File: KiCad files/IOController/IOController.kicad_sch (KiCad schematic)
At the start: 12 parts, among them J1 AVR-ISP-6, J2 Conn_01x01, J3 Conn_01x01, J4 Conn_01x01, J5 Conn_01x01, Q1 IRF3205, U1 ATtiny85-20P, U2 LP2985-5.0

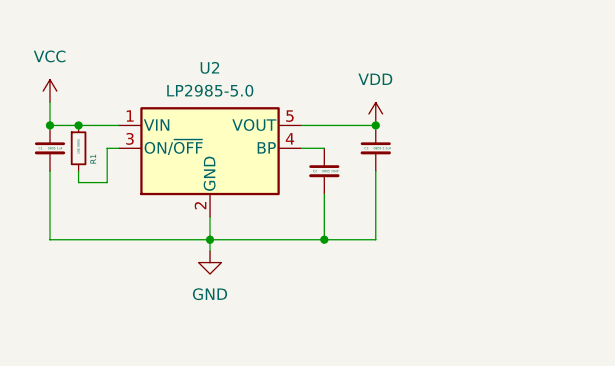
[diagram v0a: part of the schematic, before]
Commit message: swapped regulator for 1.8V instead of 5V for lower power
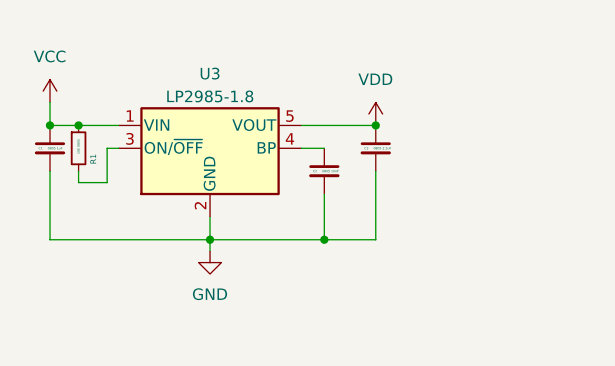
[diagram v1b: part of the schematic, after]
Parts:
- removed U2: LP2985-5.0, Package_TO_SOT_SMD:SOT-23-5, symbol Regulator_Linear:LP2985-5.0
- added U3: LP2985-1.8, Package_TO_SOT_SMD:SOT-23-5, symbol Regulator_Linear:LP2985-1.8
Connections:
- net GND: now also U3.2 (GND)
- net VCC: now also U3.1 (VIN)
- net VDD: now also U3.5 (VOUT)
- net at C2.1: now also U3.4 (BP)
- net at R1.2: now also U3.3 (ON/~{OFF})
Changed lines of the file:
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@@
+    )
+  )
+  (symbol (lib_id "Regulator_Linear:LP2985-1.8") (at 41.91 25.4 0) (unit 1)
+    (in_bom yes) (on_board yes) (dnp no) (fields_autoplaced)
+    (property "Reference" "U3" (at 41.91 17.145 0)
+      (effects (font (size 1.27 1.27)))
+    )
+    (property "Value" "LP2985-1.8" (at 41.91 19.685 0)
+      (effects (font (size 1.27 1.27)))
+    )
+    (property "Footprint" "Package_TO_SOT_SMD:SOT-23-5" (at 41.91 17.145 0)
+      (effects (font (size 1.27 1.27)) hide)
+    )
+    (property "Datasheet" "http://www.ti.com/lit/ds/symlink/lp2985.pdf" (at 41.91 25.4 0)
+      (effects (font (size 1.27 1.27)) hide)
+    )
+    (pin "3")
+    (pin "5")
+    (pin "4")
+    (pin "2")
+    (pin "1")
+    (instances
+      (project "IOController"
+        (path "/f1c719f6-f1ad-4e81-8891-bde8a483290d"
+          (reference "U3") (unit 1)
+        )
+      )
     )
   )
@@
         )
       )
-    )
-  )
-  (symbol (lib_id "Regulator_Linear:LP2985-5.0") (at 41.91 25.4 0) (unit 1)
-    (in_bom yes) (on_board yes) (dnp no) (fields_autoplaced)
-    (property "Reference" "U2" (at 41.91 16.51 0)
-      (effects (font (size 1.27 1.27)))
-    )
-    (property "Value" "LP2985-5.0" (at 41.91 19.05 0)
-      (effects (font (size 1.27 1.27)))
-    )
-    (property "Footprint" "Package_TO_SOT_SMD:SOT-23-5" (at 41.91 17.145 0)
-      (effects (font (size 1.27 1.27)) hide)
-    )
-    (property "Datasheet" "http://www.ti.com/lit/ds/symlink/lp2985.pdf" (at 41.91 25.4 0)
-      (effects (font (size 1.27 1.27)) hide)
-    )
-    (pin "4")
-    (pin "3")
-    (pin "2")
-    (pin "5")
-    (pin "1")
-    (instances
-      (project "IOController"
-        (path "/f1c719f6-f1ad-4e81-8891-bde8a483290d"
-          (reference "U2") (unit 1)
-        )
-      )

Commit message: added some parts to controller board for now.
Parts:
- removed J5: Conn_01x01, Connector_Wire:SolderWire-2.5sqmm_1x01_D2.4mm_OD3.6mm, symbol Connector_Generic:Conn_01x01
- removed Q1: IRF3205, Package_TO_SOT_THT:TO-220-3_Vertical, symbol Transistor_FET:IRF3205
- added J6: Conn_01x01, Connector_Wire:SolderWire-2.5sqmm_1x01_D2.4mm_OD3.6mm, symbol Connector_Generic:Conn_01x01
- added SW1: RotaryEncoder_Switch, Rotary_Encoder:RotaryEncoder_Bourns_Horizontal_PEC09-2xxxF-Nxxxx, symbol Device:RotaryEncoder_Switch
- added SW2: SW_Push, symbol Switch:SW_Push
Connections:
- net NPN-Gate: now also J6.1 (Pin_1)
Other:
- moved on the sheet: J2
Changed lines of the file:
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@@
+    (stroke (width 0) (type default))
+  )
+  (wire (pts (xy 146.05 34.29) (xy 146.05 32.385))
     (stroke (width 0) (type default))
   )
@@
     (stroke (width 0) (type default))
   )
-  (wire (pts (xy 135.89 25.4) (xy 135.89 23.495))
+  (wire (pts (xy 135.89 34.29) (xy 135.89 32.385))
     (stroke (width 0) (type default))
   )
@@
     (stroke (width 0) (type default))
   )
-  (wire (pts (xy 146.05 25.4) (xy 146.05 23.495))
-    (stroke (width 0) (type default))
-  )
   (wire (pts (xy 76.2 76.835) (xy 65.405 76.835))
     (stroke (width 0) (type default))
@@
     (stroke (width 0) (type default))
   )
-  (global_label "NPN-Gate" (shape input) (at 146.05 36.83 180) (fields_autoplaced)
-    (effects (font (size 1.27 1.27)) (justify right))
-    (property "Intersheetrefs" "${INTERSHEET_REFS}" (at 133.3281 36.83 0)
-      (effects (font (size 1.27 1.27)) (justify right) hide)
-    )
-  )
-  (global_label "LED_GND" (shape input) (at 153.67 31.75 90) (fields_autoplaced)
+  (global_label "NPN-Gate" (shape input) (at 146.05 32.385 90) (fields_autoplaced)
     (effects (font (size 1.27 1.27)) (justify left))
-    (property "Intersheetrefs" "${INTERSHEET_REFS}" (at 153.67 20.4796 90)
+    (property "Intersheetrefs" "${INTERSHEET_REFS}" (at 146.05 19.6631 90)
       (effects (font (size 1.27 1.27)) (justify left) hide)
     )
@@
     )
   )
-  (global_label "LED_GND" (shape input) (at 146.05 23.495 90) (fields_autoplaced)
-    (effects (font (size 1.27 1.27)) (justify left))
-    (property "Intersheetrefs" "${INTERSHEET_REFS}" (at 146.05 12.2246 90)
+  (symbol (lib_id "Connector_Generic:Conn_01x01") (at 135.89 39.37 270) (unit 1)
+    (in_bom yes) (on_board yes) (dnp no)
+    (property "Reference" "J2" (at 138.43 38.1 90)
+      (effects (font (size 1.27 1.27)) (justify left))
+    )
+    (property "Value" "Conn_01x01" (at 138.43 40.64 90)
       (effects (font (size 1.27 1.27)) (justify left) hide)
     )
-  )
-  (symbol (lib_id "Connector_Generic:Conn_01x01") (at 135.89 30.48 270) (unit 1)
-    (in_bom yes) (on_board yes) (dnp no) (fields_autoplaced)
-    (property "Reference" "J2" (at 138.43 29.21 90)
-      (effects (font (size 1.27 1.27)) (justify left))
-    )
-    (property "Value" "Conn_01x01" (at 138.43 31.75 90)
-      (effects (font (size 1.27 1.27)) (justify left) hide)
-    )
-    (property "Footprint" "Connector_Wire:SolderWire-2.5sqmm_1x01_D2.4mm_OD3.6mm" (at 135.89 30.48 0)
-      (effects (font (size 1.27 1.27)) hide)
-    )
-    (property "Datasheet" "~" (at 135.89 30.48 0)
+    (property "Footprint" "Connector_Wire:SolderWire-2.5sqmm_1x01_D2.4mm_OD3.6mm" (at 135.89 39.37 0)
+      (effects (font (size 1.27 1.27)) hide)
+    )
+    (property "Datasheet" "~" (at 135.89 39.37 0)
       (effects (font (size 1.27 1.27)) hide)
     )
@@
     )
   )
+  (symbol (lib_id "Switch:SW_Push") (at 132.08 98.425 0) (unit 1)
+    (in_bom yes) (on_board yes) (dnp no) (fields_autoplaced)
+    (property "Reference" "SW2" (at 132.08 90.17 0)
+      (effects (font (size 1.27 1.27)))
+    )
+    (property "Value" "SW_Push" (at 132.08 92.71 0)
+      (effects (font (size 1.27 1.27)))
+    )
+    (property "Footprint" "" (at 132.08 93.345 0)
+      (effects (font (size 1.27 1.27)) hide)
+    )
+    (property "Datasheet" "~" (at 132.08 93.345 0)
+      (effects (font (size 1.27 1.27)) hide)
+    )
+    (pin "2")
+    (pin "1")
+    (instances
+      (project "IOController"
+        (path "/f1c719f6-f1ad-4e81-8891-bde8a483290d"
+          (reference "SW2") (unit 1)
+        )
+      )
+    )
+  )
   (symbol (lib_id "power:GND") (at 50.165 86.995 0) (unit 1)
     (in_bom yes) (on_board yes) (dnp no) (fields_autoplaced)
@@
         (path "/f1c719f6-f1ad-4e81-8891-bde8a483290d"
           (reference "#PWR02") (unit 1)
-        )
-      )
-    )
-  )
-  (symbol (lib_id "Connector_Generic:Conn_01x01") (at 146.05 30.48 270) (unit 1)
-    (in_bom yes) (on_board yes) (dnp no) (fields_autoplaced)
-    (property "Reference" "J5" (at 148.59 29.21 90)
-      (effects (font (size 1.27 1.27)) (justify left))
-    )
-    (property "Value" "Conn_01x01" (at 148.59 31.75 90)
-      (effects (font (size 1.27 1.27)) (justify left) hide)
-    )
-    (property "Footprint" "Connector_Wire:SolderWire-2.5sqmm_1x01_D2.4mm_OD3.6mm" (at 146.05 30.48 0)
-      (effects (font (size 1.27 1.27)) hide)
-    )
-    (property "Datasheet" "~" (at 146.05 30.48 0)
-      (effects (font (size 1.27 1.27)) hide)
-    )
-    (pin "1")
-    (instances
-      (project "IOController"
-        (path "/f1c719f6-f1ad-4e81-8891-bde8a483290d"
-          (reference "J5") (unit 1)
         )
       )
@@
     )
   )
-  (symbol (lib_id "power:VCC") (at 135.89 23.495 0) (unit 1)
-    (in_bom yes) (on_board yes) (dnp no) (fields_autoplaced)
-    (property "Reference" "#PWR08" (at 135.89 27.305 0)
-      (effects (font (size 1.27 1.27)) hide)
-    )
-    (property "Value" "VCC" (at 135.89 18.415 0)
-      (effects (font (size 1.27 1.27)))
-    )
-    (property "Footprint" "" (at 135.89 23.495 0)
-      (effects (font (size 1.27 1.27)) hide)
-    )
-    (property "Datasheet" "" (at 135.89 23.495 0)
+  (symbol (lib_id "power:VCC") (at 135.89 32.385 0) (unit 1)
+    (in_bom yes) (on_board yes) (dnp no) (fields_autoplaced)
+    (property "Reference" "#PWR08" (at 135.89 36.195 0)
+      (effects (font (size 1.27 1.27)) hide)
+    )
+    (property "Value" "VCC" (at 135.89 27.305 0)
+      (effects (font (size 1.27 1.27)))
+    )
+    (property "Footprint" "" (at 135.89 32.385 0)
+      (effects (font (size 1.27 1.27)) hide)
+    )
+    (property "Datasheet" "" (at 135.89 32.385 0)
       (effects (font (size 1.27 1.27)) hide)
     )
@@
     )
   )
-  (symbol (lib_id "Transistor_FET:IRF3205") (at 151.13 36.83 0) (unit 1)
-    (in_bom yes) (on_board yes) (dnp no) (fields_autoplaced)
-    (property "Reference" "Q1" (at 157.48 35.56 0)
+  (symbol (lib_id "Connector_Generic:Conn_01x01") (at 146.05 39.37 270) (unit 1)
+    (in_bom yes) (on_board yes) (dnp no)
+    (property "Reference" "J6" (at 148.59 38.1 90)
       (effects (font (size 1.27 1.27)) (justify left))
     )
-    (property "Value" "IRF3205" (at 157.48 38.1 0)
-      (effects (font (size 1.27 1.27)) (justify left))
-    )
-    (property "Footprint" "Package_TO_SOT_THT:TO-220-3_Vertical" (at 156.21 38.735 0)
-      (effects (font (size 1.27 1.27) italic) (justify left) hide)
-    )
-    (property "Datasheet" "http://www.irf.com/product-info/datasheets/data/irf3205.pdf" (at 156.21 40.64 0)
+    (property "Value" "Conn_01x01" (at 148.59 40.64 90)
       (effects (font (size 1.27 1.27)) (justify left) hide)
     )
-    (pin "2")
-    (pin "1")
-    (pin "3")
-    (instances
-      (project "IOController"
-        (path "/f1c719f6-f1ad-4e81-8891-bde8a483290d"
-          (reference "Q1") (unit 1)
+    (property "Footprint" "Connector_Wire:SolderWire-2.5sqmm_1x01_D2.4mm_OD3.6mm" (at 146.05 39.37 0)
+      (effects (font (size 1.27 1.27)) hide)
+    )
+    (property "Datasheet" "~" (at 146.05 39.37 0)
+      (effects (font (size 1.27 1.27)) hide)
+    )
+    (pin "1")
+    (instances
+      (project "IOController"
+        (path "/f1c719f6-f1ad-4e81-8891-bde8a483290d"
+          (reference "J6") (unit 1)
         )
       )
@@
     )
   )
+  (symbol (lib_id "Device:RotaryEncoder_Switch") (at 117.475 79.375 90) (unit 1)
+    (in_bom yes) (on_board yes) (dnp no) (fields_autoplaced)
+    (property "Reference" "SW1" (at 124.46 78.105 90)
+      (effects (font (size 1.27 1.27)) (justify right))
+    )
+    (property "Value" "RotaryEncoder_Switch" (at 124.46 80.645 90)
+      (effects (font (size 1.27 1.27)) (justify right))
+    )
+    (property "Footprint" "Rotary_Encoder:RotaryEncoder_Bourns_Horizontal_PEC09-2xxxF-Nxxxx" (at 113.411 83.185 0)
+      (effects (font (size 1.27 1.27)) hide)
+    )
+    (property "Datasheet" "~" (at 110.871 79.375 0)
+      (effects (font (size 1.27 1.27)) hide)
+    )
+    (pin "S2")
+    (pin "B")
+    (pin "S1")
+    (pin "A")
+    (pin "C")
+    (instances
+      (project "IOController"
+        (path "/f1c719f6-f1ad-4e81-8891-bde8a483290d"
+          (reference "SW1") (unit 1)
+        )
+      )
+    )
+  )
   (symbol (lib_id "power:VDD") (at 50.165 56.515 0) (unit 1)
     (in_bom yes) (on_board yes) (dnp no) (fields_autoplaced)
@@
         )
       )
-    )
-  )
-  (symbol (lib_id "power:GND") (at 153.67 41.91 0) (unit 1)
-    (in_bom yes) (on_board yes) (dnp no) (fields_autoplaced)
-    (property "Reference" "#PWR011" (at 153.67 48.26 0)
-      (effects (font (size 1.27 1.27)) hide)
-    )
-    (property "Value" "GND" (at 153.67 46.99 0)
-      (effects (font (size 1.27 1.27)))
-    )
-    (property "Footprint" "" (at 153.67 41.91 0)
-      (effects (font (size 1.27 1.27)) hide)
-    )
-    (property "Datasheet" "" (at 153.67 41.91 0)
-      (effects (font (size 1.27 1.27)) hide)
-    )
-    (pin "1")
-    (instances
-      (project "IOController"
-        (path "/f1c719f6-f1ad-4e81-8891-bde8a483290d"
-          (reference "#PWR011") (unit 1)
-        )
-      )

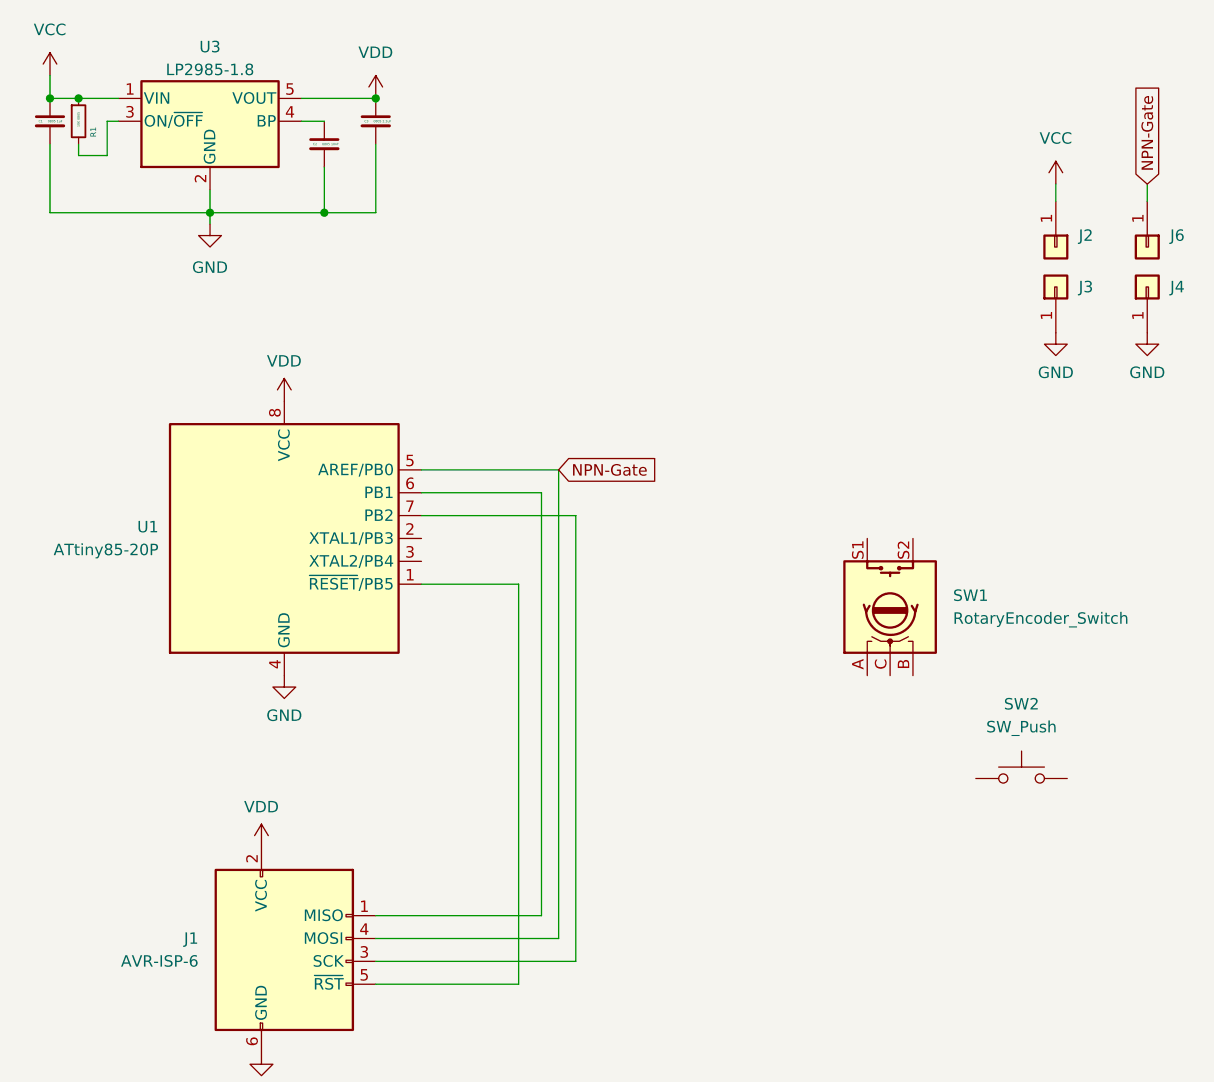
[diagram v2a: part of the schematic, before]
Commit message: modified IO board and LED board so they connect together using XT60
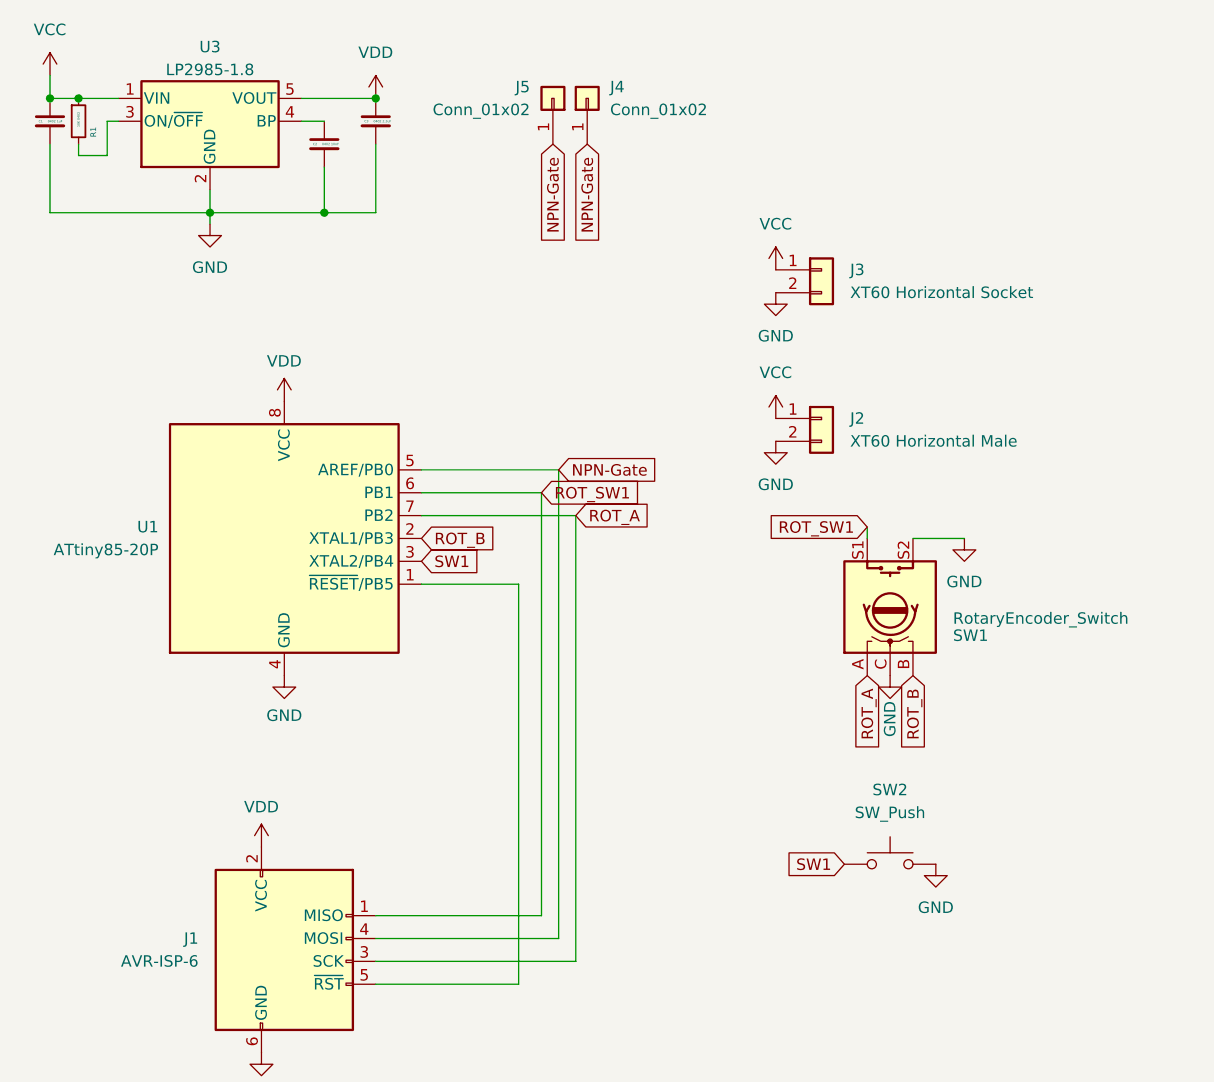
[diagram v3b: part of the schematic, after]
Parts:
- removed J2, J3, J6: Conn_01x01, Connector_Wire:SolderWire-2.5sqmm_1x01_D2.4mm_OD3.6mm, symbol Connector_Generic:Conn_01x01
- added J2: XT60 Horizontal Male, Connector_AMASS:AMASS_XT60PW-M_1x02_P7.20mm_Horizontal, symbol Connector_Generic:Conn_01x02
- added J3: XT60 Horizontal Socket, Connector_AMASS:AMASS_XT60PW-F_1x02_P7.20mm_Horizontal, symbol Connector_Generic:Conn_01x02
- added J5: Conn_01x02, Connector_PinHeader_2.54mm:PinHeader_1x01_P2.54mm_Horizontal, symbol Connector_Generic:Conn_01x01
- C1: value 0805 1uF -> 0402 1uF; footprint (none) -> Capacitor_SMD:C_0402_1005Metric
- C2: value 0805 10nF -> 0402 10nF; footprint (none) -> Capacitor_SMD:C_0402_1005Metric
- C3: value 0805 2.2uF -> 0402 2.2uF; footprint (none) -> Capacitor_SMD:C_0402_1005Metric
- J1: footprint (none) -> Connector_PinHeader_1.00mm:PinHeader_2x03_P1.00mm_Vertical
- J4: value Conn_01x01 -> Conn_01x02; footprint Connector_Wire:SolderWire-2.5sqmm_1x01_D2.4mm_OD3.6mm -> Connector_PinHeader_2.54mm:PinHeader_1x01_P2.54mm_Horizontal
- R1: value 10K 0805 -> 10K 0402; footprint (none) -> Resistor_SMD:R_0402_1005Metric
- SW1: footprint Rotary_Encoder:RotaryEncoder_Bourns_Horizontal_PEC09-2xxxF-Nxxxx -> Rotary_Encoder:RotaryEncoder_Alps_EC12E-Switch_Vertical_H20mm_CircularMountingHoles
- SW2: footprint (none) -> Button_Switch_SMD:SW_SPST_B3U-1000P
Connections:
- net GND: now also SW1.C, SW1.S2, SW2.2, J2.2 (Pin_2), J3.2 (Pin_2); no longer J4.1 (Pin_1)
- net NPN-Gate: now also J4.1 (Pin_1), J5.1 (Pin_1)
- net VCC: now also J2.1 (Pin_1), J3.1 (Pin_1)
- net ROT_B: now reaches U1.2 (XTAL1/PB3)
- net ROT_B: now also SW1.B
- net SW1: now reaches U1.3 (XTAL2/PB4)
- net SW1: now also SW2.1
- net ROT_SW1: now reaches J1.1 (MISO), U1.6 (PB1)
- net ROT_SW1: now also SW1.S1
- net ROT_A: now reaches J1.3 (SCK), U1.7 (PB2)
- net ROT_A: now also SW1.A
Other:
- moved on the sheet: SW2
